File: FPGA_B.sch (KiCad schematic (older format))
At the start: 8 parts, among them Q13 2N7002BK, Q9 2N7002BK

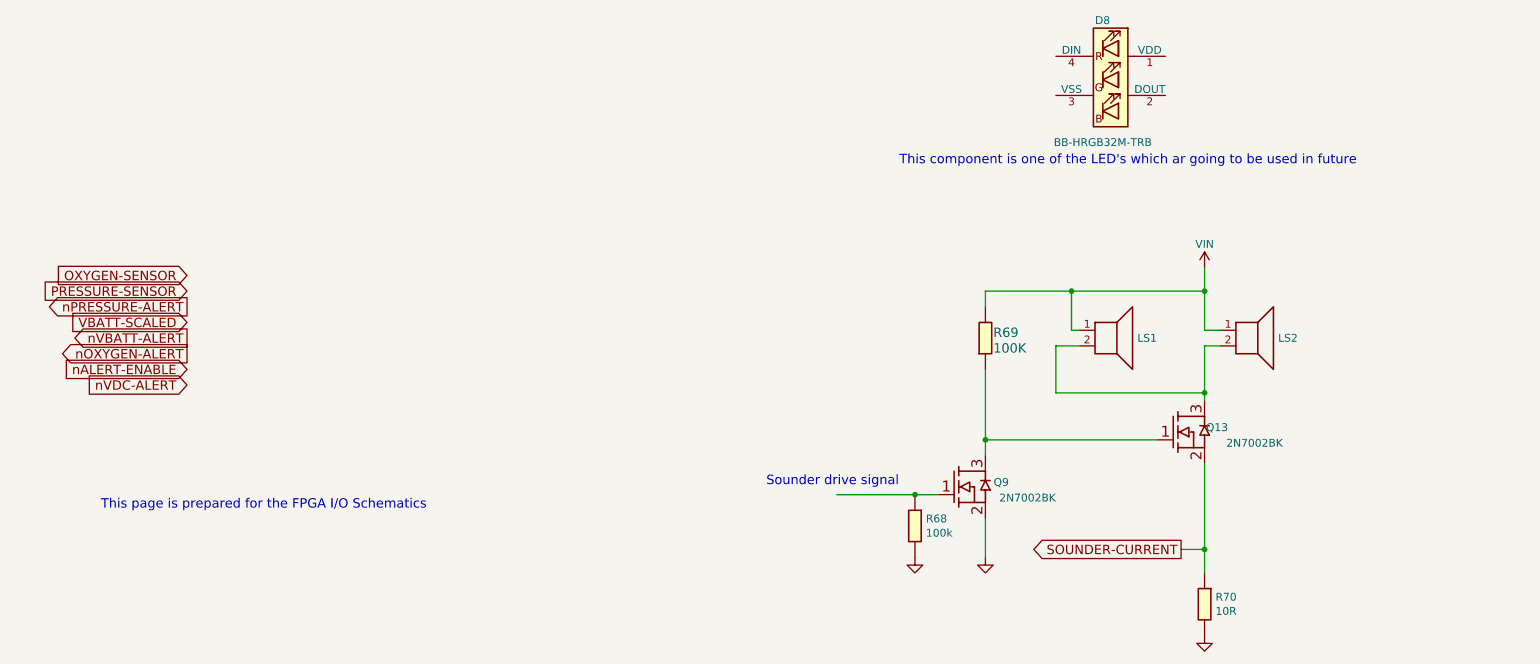
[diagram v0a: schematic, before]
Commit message: Still had some text cleanups to do plus fixed a couple of minor circuit issues.
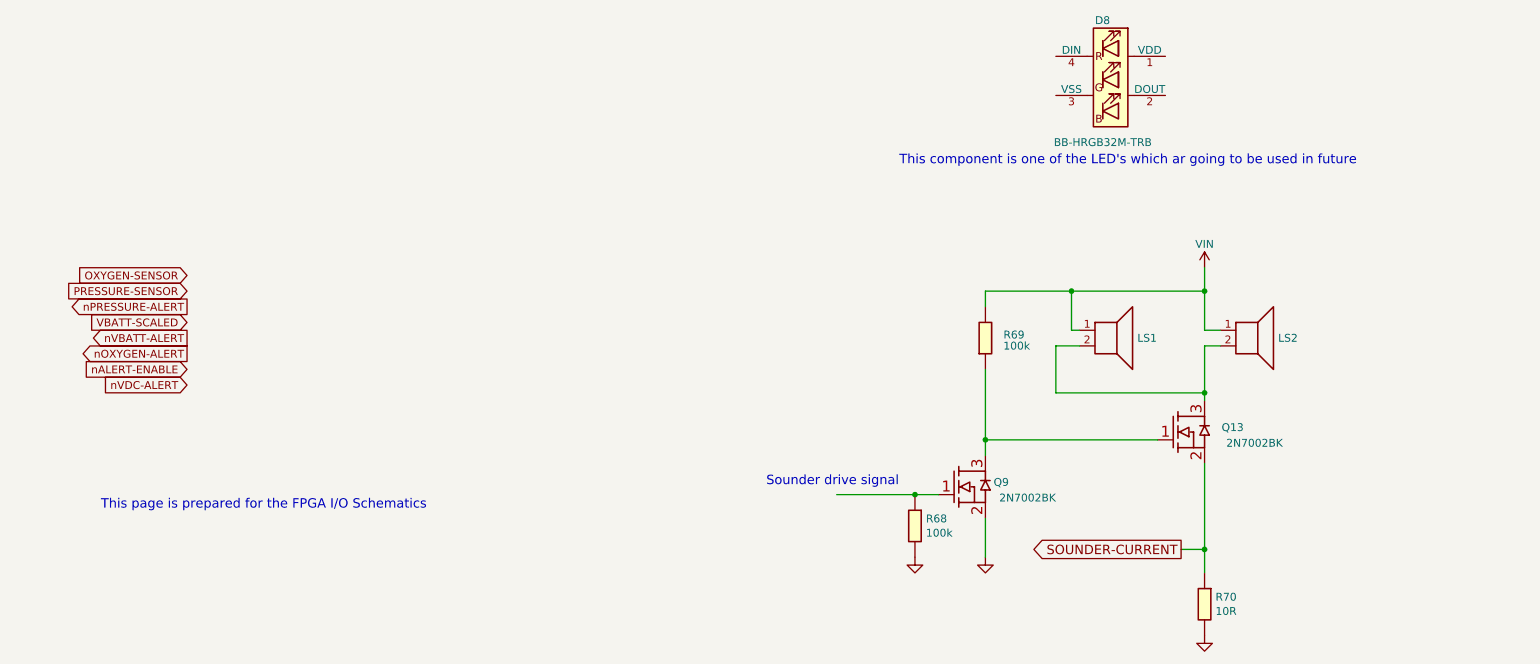
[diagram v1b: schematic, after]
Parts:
- R69: value 100K -> 100K_0603_Chip_Resistor,_1%,_0.1W; Val (none) -> 100k; Watt (none) -> 0.1W
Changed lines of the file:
@@
 Comment4 ""
 $EndDescr
-Text GLabel 1750 3100 0    60   Input ~ 0
+Text GLabel 1750 3100 0    50   Input ~ 0
 PRESSURE-SENSOR
-Text GLabel 1750 3000 0    60   Input ~ 0
+Text GLabel 1750 3000 0    50   Input ~ 0
 OXYGEN-SENSOR
-Text GLabel 1750 3600 0    60   Input ~ 0
+Text GLabel 1750 3600 0    50   Input ~ 0
 nALERT-ENABLE
-Text GLabel 1750 3300 0    60   Input ~ 0
+Text GLabel 1750 3300 0    50   Input ~ 0
 VBATT-SCALED
-Text GLabel 1750 3200 0    60   Output ~ 0
+Text GLabel 1750 3200 0    50   Output ~ 0
 nPRESSURE-ALERT
-Text GLabel 1750 3500 0    60   Output ~ 0
+Text GLabel 1750 3500 0    50   Output ~ 0
 nOXYGEN-ALERT
-Text GLabel 1750 3400 0    60   Output ~ 0
+Text GLabel 1750 3400 0    50   Output ~ 0
 nVBATT-ALERT
-Text GLabel 1750 3700 0    60   Input ~ 0
+Text GLabel 1750 3700 0    50   Input ~ 0
 nVDC-ALERT
 $Comp
@@
 U 1 1 5F8DD181
 P 8250 3800
-F 0 "Q13" H 8100 3600 50  0000 L BNN
+F 0 "Q13" H 8000 3600 50  0000 L BNN
 F 1 "2N7002BK" H 7750 3500 50  0000 L BNN
 F 2 "" H 8200 3450 50  0001 C CNN
@@
 U 1 1 5F8DD180
 P 6750 3500
-F 0 "R69" V 6850 3350 60  0000 R TNN
-F 1 "100K" V 6750 3350 60  0000 R TNN
-F 2 "" H 6650 3360 60  0000 C CNN
-F 3 "" H 6650 3360 60  0000 C CNN
-F 4 "1%" V -1000 -2650 60  0001 C CNN "Tolerance"
+F 0 "R69" V 6900 3150 50  0000 L BNN
+F 1 "100K_0603_Chip_Resistor,_1%,_0.1W" V 6750 3350 50  0001 C CNN
+F 2 "" H 6650 3360 50  0001 C CNN
+F 3 "" H 6650 3360 50  0001 C CNN
+F 4 "1%" V -1000 -2650 50  0001 C CNN "Tolerance"
+F 5 "100k" V 6800 3200 50  0000 C CNN "Val"
+F 6 "0.1W" H 6750 3500 50  0001 C CNN "Watt"
 	1    6750 3500
 	0    -1   -1   0
